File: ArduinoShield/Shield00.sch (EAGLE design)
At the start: 28 parts

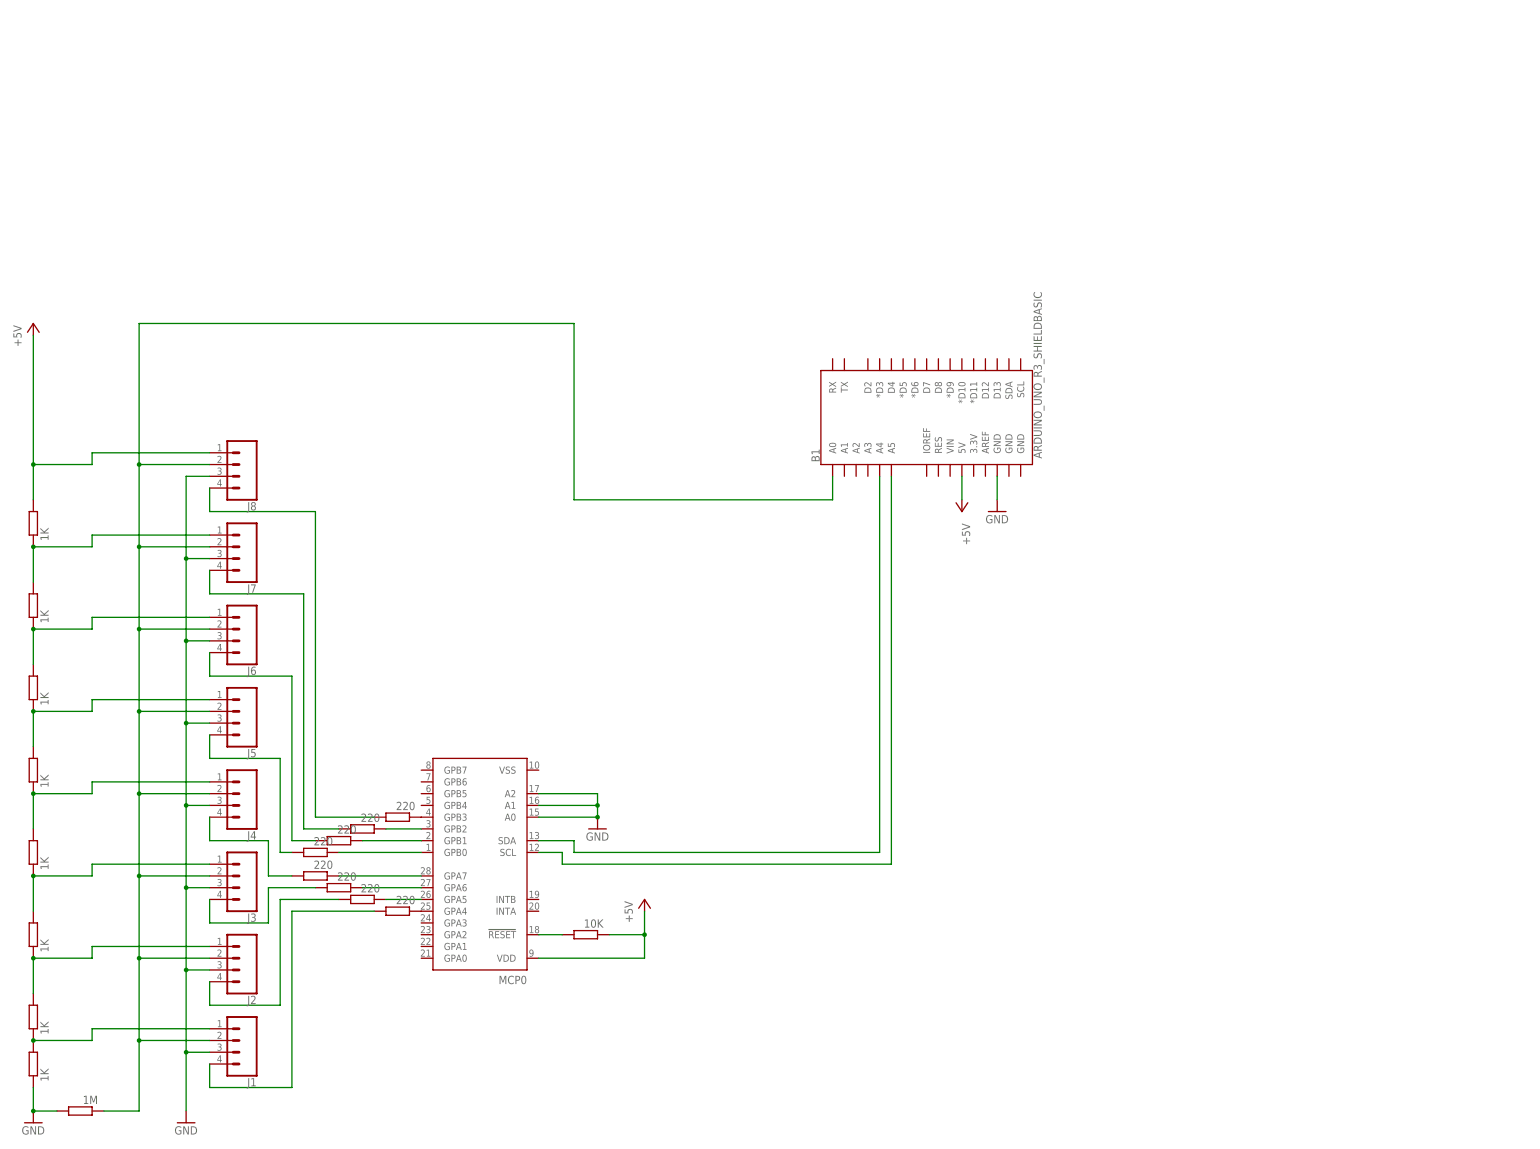
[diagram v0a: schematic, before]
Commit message: add mp3, mcp1 et 2 and pumplevel
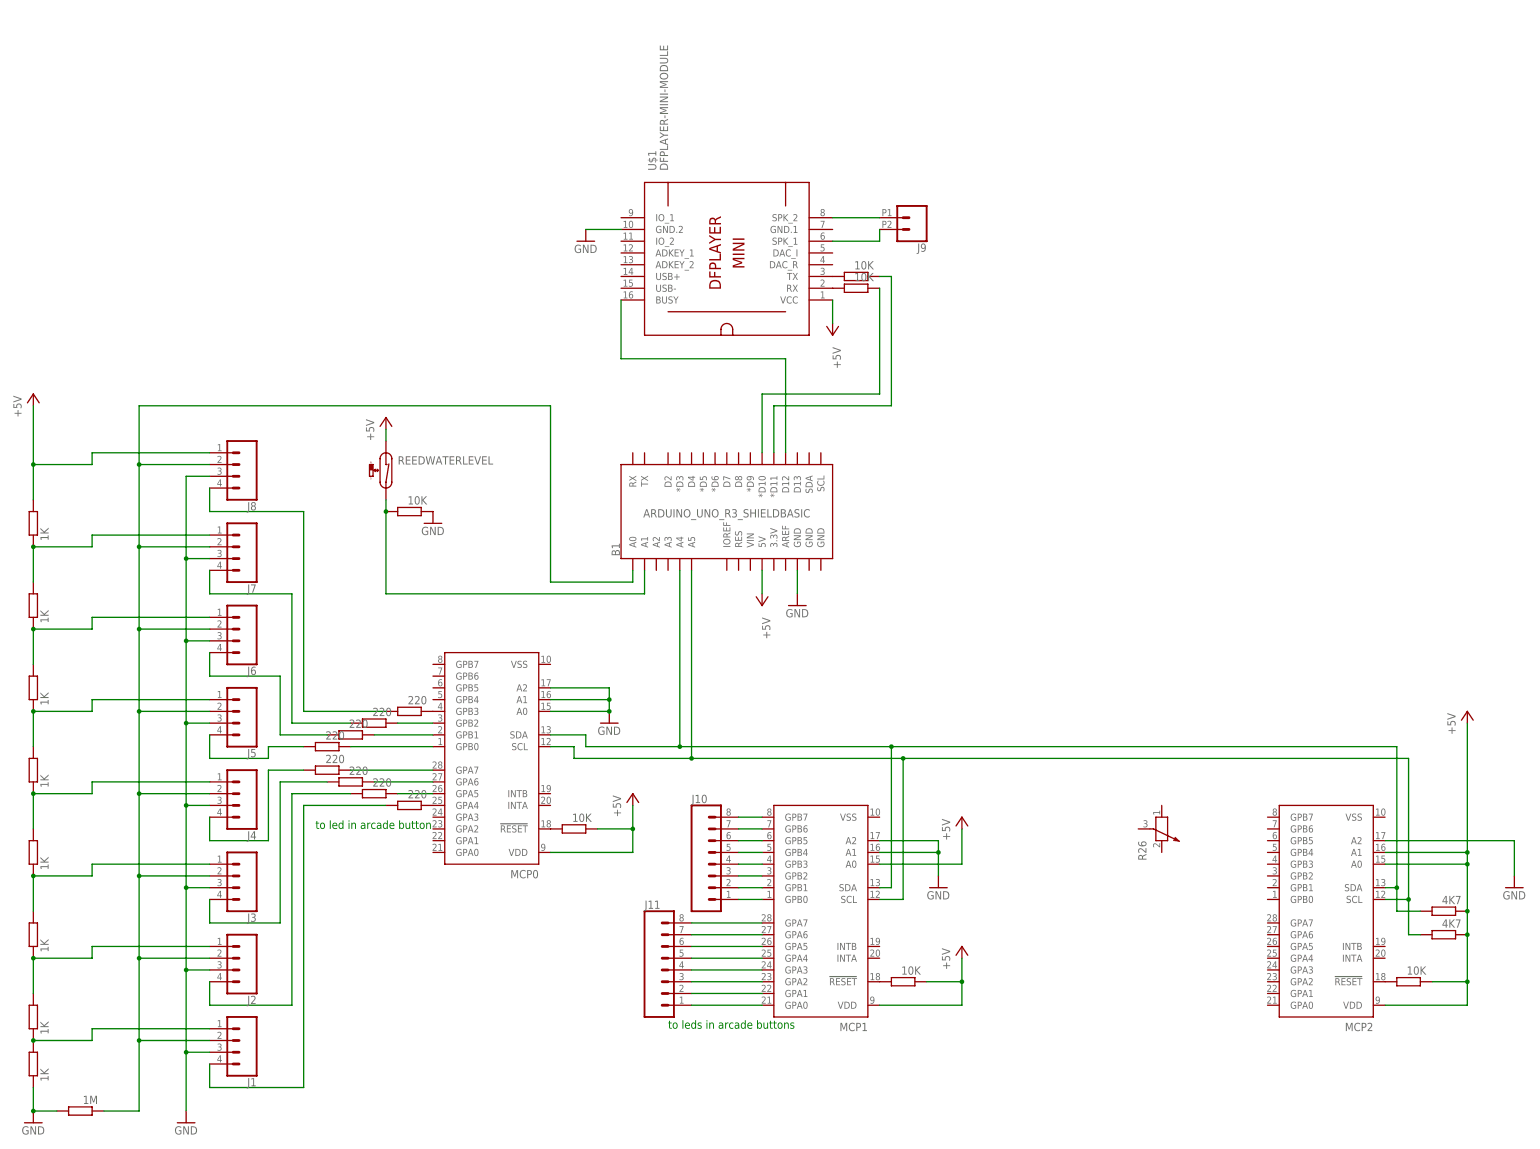
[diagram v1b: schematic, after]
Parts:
- added J10, J11: (no value), SparkFun-Connectors:CONN_08"
- added J9: (no value), SparkFun-Connectors:CONN_022.54MM_SCREWTERM
- added MCP1, MCP2: MCP23017SO, microchip:MCP23017SO
- added R10, R19, R21, R22, R23: 10K, rcl:R-EU_R0805
- added R24, R25: 4K7, rcl:R-EU_R0805
- added R26: (no value), rcl:POTENTIOMETER_PT-10
- added REEDWATERLEVEL: REED-SWITCH-MK6-5-B, switch-reed:REED-SWITCH-MK6-5-B
- added U$1: DFPLAYER-MINI-MODULE, diy-modules:DFPLAYER-MINI-MODULE
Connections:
- new net N$18: B1.A4, MCP0.SDA, MCP1.SDA, MCP2.SDA, R24.2
- new net N$26: J9.1, U$1.SPK_2
- new net N$27: J9.2, U$1.SPK_1
- new net N$28: R10.2, U$1.TX
- new net N$32: B1.*D10, R19.1
- new net N$33: B1.*D11, R10.1
- new net N$34: B1.D12, U$1.BUSY
- new net N$35: MCP1.!RESET, R22.2
- new net N$36: B1.A1, R21.2, REEDWATERLEVEL.2
- new net N$37: J10.5, MCP1.GPB4
- new net N$38: J10.4, MCP1.GPB3
- new net N$39: J10.3, MCP1.GPB2
- new net N$40: J10.2, MCP1.GPB1
- new net N$41: J10.1, MCP1.GPB0
- new net N$42: J11.8, MCP1.GPA7
- new net N$43: J11.7, MCP1.GPA6
- new net N$44: J11.6, MCP1.GPA5
- new net N$45: J11.5, MCP1.GPA4
- new net N$46: J11.4, MCP1.GPA3
- new net N$47: J11.3, MCP1.GPA2
- new net N$48: J11.2, MCP1.GPA1
- new net N$49: J11.1, MCP1.GPA0
- new net N$50: J10.6, MCP1.GPB5
- new net N$51: J10.7, MCP1.GPB6
- new net N$52: J10.8, MCP1.GPB7
- new net N$55: MCP2.!RESET, R23.2
- net +5V: now also MCP1.A0, MCP1.VDD, MCP2.A0, MCP2.A1, MCP2.VDD, R22.1, R23.1, R24.1, R25.1, REEDWATERLEVEL.1, U$1.VCC
- net GND: now also MCP1.A1, MCP1.A2, MCP2.A2, R21.1, U$1.GND.2
- net N$29: now also MCP1.SCL, MCP2.SCL, R25.2
- net N$31: now also R19.2, U$1.RX; no longer B1.A4, MCP0.SDA
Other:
- note added: "to led in arcade button"
- note added: "to leds in arcade buttons"
- moved on the sheet: B1, MCP0

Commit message: end v1 schemboard
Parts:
- removed J10: (no value), SparkFun-Connectors:CONN_08"
- added J12: (no value), SparkFun-Connectors:CONN_08"
- added LED1, LED2, LED3, LED4, LED5, LED7: (no value), led:LED5MM
- added R27, R28, R29, R30, R31, R32, R33, R34, R35, R36, R37, R38, R39, R40, R41, R42: 10K, rcl:R-EU_R0805
- added R43, R44, R45, R46, R48: (no value), rcl:POTENTIOMETER_PT-10
- added T1, T10, T11, T12, T13, T14, T15, T16, T2, T3, T4, T5, T6, T7, T8, T9: BC337, transistor:BC337
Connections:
- new net N$53: R34.1, T8.B
- new net N$54: R36.1, T10.B
- new net N$56: R37.1, T11.B
- new net N$57: R38.1, T12.B
- new net N$58: R39.1, T13.B
- new net N$59: R40.1, T14.B
- new net N$60: R41.1, T15.B
- new net N$61: R42.1, T16.B
- new net N$62: MCP1.GPA7, R34.2
- new net N$63: MCP1.GPA6, R33.2
- new net N$64: MCP1.GPA5, R32.2
- new net N$65: MCP1.GPA4, R31.2
- new net N$66: MCP1.GPA3, R30.2
- new net N$67: MCP1.GPA2, R29.2
- new net N$68: MCP1.GPA1, R28.2
- new net N$69: MCP1.GPA0, R27.2
- new net N$70: J11.4, T4.C
- new net N$71: J11.5, T5.C
- new net N$72: J11.6, T6.C
- new net N$73: J11.7, T7.C
- new net N$74: J11.8, T8.C
- new net N$75: J11.3, T3.C
- new net N$76: J11.2, T2.C
- new net N$77: J11.1, T1.C
- new net N$78: J12.4, T12.C
- new net N$79: J12.5, T13.C
- new net N$80: J12.6, T14.C
- new net N$81: J12.7, T15.C
- new net N$82: J12.8, T16.C
- new net N$83: J12.3, T11.C
- new net N$84: J12.2, T10.C
- new net N$85: J12.1, T9.C
- new net N$86: MCP2.GPA0, R48.1
- new net N$87: LED1.A, R26.3
- new net N$88: MCP2.GPA1, R26.1
- new net N$89: LED2.A, R43.3
- new net N$90: MCP2.GPA2, R43.1
- new net N$91: LED3.A, R44.3
- new net N$92: MCP2.GPA3, R44.1
- new net N$93: LED4.A, R45.3
- new net N$94: MCP2.GPA4, R45.1
- new net N$95: LED5.A, R46.3
- new net N$96: MCP2.GPA5, R46.1
- new net N$98: LED7.A, R48.3
- net GND: now also LED1.C, LED2.C, LED3.C, LED4.C, LED5.C, LED7.C, R26.2, R43.2, R44.2, R45.2, R46.2, R48.2, T1.E, T10.E, T11.E, T12.E, T13.E, T14.E, T15.E, T16.E, T2.E, T3.E, T4.E, T5.E, T6.E, T7.E, T8.E, T9.E
- net N$37: now also R39.2; no longer J10.5
- net N$38: now also R38.2; no longer J10.4
- net N$39: now also R37.2; no longer J10.3
- net N$40: now also R36.2; no longer J10.2
- net N$41: now also R35.2; no longer J10.1
- net N$42: now also R32.1, T6.B; no longer J11.8, MCP1.GPA7
- net N$43: now also R35.1, T9.B; no longer J11.7, MCP1.GPA6
- net N$44: now also R27.1, T1.B; no longer J11.6, MCP1.GPA5
- net N$45: now also R28.1, T2.B; no longer J11.5, MCP1.GPA4
- net N$46: now also R30.1, T4.B; no longer J11.4, MCP1.GPA3
- net N$47: now also R29.1, T3.B; no longer J11.3, MCP1.GPA2
- net N$48: now also R31.1, T5.B; no longer J11.2, MCP1.GPA1
- net N$49: now also R33.1, T7.B; no longer J11.1, MCP1.GPA0
- net N$50: now also R40.2; no longer J10.6
- net N$51: now also R41.2; no longer J10.7
- net N$52: now also R42.2; no longer J10.8
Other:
- note added: "To relays, 2x module 8"
- note removed: "to leds in arcade buttons"
- moved on the sheet: J11, MCP1, MCP2, R26

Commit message: pump still not working
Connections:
- net N$36: now also B1.D8; no longer B1.A1
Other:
- moved on the sheet: REEDWATERLEVEL
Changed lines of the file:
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@@
 <attribute name="VALUE" x="375.92" y="106.68" size="1.778" layer="96"/>
 </instance>
-<instance part="REEDWATERLEVEL" gate="G$1" x="289.56" y="137.16" smashed="yes">
-<attribute name="NAME" x="292.1" y="139.7" size="1.778" layer="95"/>
+<instance part="REEDWATERLEVEL" gate="G$1" x="287.02" y="193.04" smashed="yes">
+<attribute name="NAME" x="289.56" y="195.58" size="1.778" layer="95"/>
 </instance>
 <instance part="U$1" gate="G$1" x="363.22" y="185.42" smashed="yes" rot="R90">
@@
 <attribute name="VALUE" x="330.2" y="185.42" size="1.778" layer="96"/>
 </instance>
-<instance part="P+5" gate="1" x="289.56" y="149.86" smashed="yes">
-<attribute name="VALUE" x="287.02" y="144.78" size="1.778" layer="96" rot="R90"/>
-</instance>
-<instance part="R21" gate="G$1" x="294.64" y="129.54" smashed="yes" rot="R180">
-<attribute name="NAME" x="298.45" y="128.0414" size="1.778" layer="95" rot="R180" display="off"/>
-<attribute name="VALUE" x="298.45" y="132.842" size="1.778" layer="96" rot="R180"/>
-</instance>
-<instance part="GND6" gate="1" x="299.72" y="127" smashed="yes">
-<attribute name="VALUE" x="297.18" y="124.46" size="1.778" layer="96"/>
+<instance part="P+5" gate="1" x="287.02" y="205.74" smashed="yes">
+<attribute name="VALUE" x="284.48" y="200.66" size="1.778" layer="96" rot="R90"/>
+</instance>
+<instance part="R21" gate="G$1" x="292.1" y="185.42" smashed="yes" rot="R180">
+<attribute name="NAME" x="295.91" y="183.9214" size="1.778" layer="95" rot="R180" display="off"/>
+<attribute name="VALUE" x="295.91" y="188.722" size="1.778" layer="96" rot="R180"/>
+</instance>
+<instance part="GND6" gate="1" x="297.18" y="182.88" smashed="yes">
+<attribute name="VALUE" x="294.64" y="180.34" size="1.778" layer="96"/>
 </instance>
 <instance part="MCP1" gate="G$1" x="414.02" y="10.16" smashed="yes" rot="R180">
@@
 <segment>
 <pinref part="REEDWATERLEVEL" gate="G$1" pin="1"/>
-<wire x1="289.56" y1="144.78" x2="289.56" y2="147.32" width="0.1524" layer="91"/>
+<wire x1="287.02" y1="200.66" x2="287.02" y2="203.2" width="0.1524" layer="91"/>
 <pinref part="P+5" gate="1" pin="+5V"/>
 </segment>
@@
 <segment>
 <pinref part="REEDWATERLEVEL" gate="G$1" pin="2"/>
-<wire x1="289.56" y1="132.08" x2="289.56" y2="129.54" width="0.1524" layer="91"/>
-<pinref part="B1" gate="G$1" pin="A1"/>
-<wire x1="289.56" y1="129.54" x2="289.56" y2="111.76" width="0.1524" layer="91"/>
-<wire x1="289.56" y1="111.76" x2="345.44" y2="111.76" width="0.1524" layer="91"/>
-<wire x1="345.44" y1="111.76" x2="345.44" y2="116.84" width="0.1524" layer="91"/>
+<wire x1="287.02" y1="187.96" x2="287.02" y2="185.42" width="0.1524" layer="91"/>
+<wire x1="287.02" y1="185.42" x2="287.02" y2="154.94" width="0.1524" layer="91"/>
 <pinref part="R21" gate="G$1" pin="2"/>
-<junction x="289.56" y="129.54"/>
-</segment>
-</net>
+<junction x="287.02" y="185.42"/>
+<wire x1="287.02" y1="154.94" x2="365.76" y2="154.94" width="0.1524" layer="91"/>
+<pinref part="B1" gate="G$1" pin="D8"/>
+<wire x1="365.76" y1="154.94" x2="365.76" y2="142.24" width="0.1524" layer="91"/>
+</segment>
+</net>

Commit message: add relais 0-16
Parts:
- added IRFZ44N: IRF840, transistor-fet:IRF840
- added SP1: SMS-1308MS-2-R, speaker:SMS-1308MS-2-R
- added STRIPLED: (no value), led:LED5MM
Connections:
- new net +12V: STRIPLED.A
- new net N$100: IRFZ44N.D, STRIPLED.C
- new net N$97: B1.*D9, IRFZ44N.G
- net GND: now also IRFZ44N.S
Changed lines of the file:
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@@
 <part name="R46" library="rcl" library_urn="urn:adsk.eagle:library:334" deviceset="POTENTIOMETER_" device="PT-10" package3d_urn="urn:adsk.eagle:package:23786/1"/>
 <part name="LED5" library="led" library_urn="urn:adsk.eagle:library:259" deviceset="LED" device="5MM" package3d_urn="urn:adsk.eagle:package:15799/2"/>
+<part name="IRFZ44N" library="transistor-fet" library_urn="urn:adsk.eagle:library:396" deviceset="IRF840" device="" package3d_urn="urn:adsk.eagle:package:28520/1"/>
+<part name="SP1" library="speaker" library_urn="urn:adsk.eagle:library:365" deviceset="SMS-1308MS-2-R" device="" package3d_urn="urn:adsk.eagle:package:26519/1"/>
+<part name="STRIPLED" library="led" library_urn="urn:adsk.eagle:library:259" deviceset="LED" device="5MM" package3d_urn="urn:adsk.eagle:package:15799/2"/>
+<part name="P+8" library="supply1" library_urn="urn:adsk.eagle:library:371" deviceset="+12V" device=""/>
+<part name="GND12" library="supply1" library_urn="urn:adsk.eagle:library:371" deviceset="GND" device=""/>
 </parts>
 <sheets>
@@
 <attribute name="NAME" x="483.616" y="8.128" size="1.778" layer="95" rot="R90"/>
 <attribute name="VALUE" x="485.775" y="8.128" size="1.778" layer="96" rot="R90"/>
+</instance>
+<instance part="IRFZ44N" gate="G$1" x="457.2" y="160.02" smashed="yes">
+<attribute name="NAME" x="445.77" y="162.56" size="1.778" layer="95"/>
+</instance>
+<instance part="SP1" gate="A" x="414.02" y="193.04" smashed="yes">
+<attribute name="NAME" x="419.1" y="194.31" size="1.778" layer="95"/>
+<attribute name="VALUE" x="419.1" y="190.5" size="1.778" layer="96"/>
+</instance>
+<instance part="STRIPLED" gate="G$1" x="464.82" y="175.26" smashed="yes">
+<attribute name="NAME" x="468.376" y="170.688" size="1.778" layer="95" rot="R90"/>
+<attribute name="VALUE" x="470.535" y="170.688" size="1.778" layer="96" rot="R90"/>
+</instance>
+<instance part="P+8" gate="1" x="464.82" y="187.96" smashed="yes">
+<attribute name="VALUE" x="462.28" y="182.88" size="1.778" layer="96" rot="R90"/>
+</instance>
+<instance part="GND12" gate="1" x="462.28" y="152.4" smashed="yes">
+<attribute name="VALUE" x="459.74" y="149.86" size="1.778" layer="96"/>
 </instance>
 </instances>
@@
 <junction x="480.06" y="7.62"/>
 </segment>
+<segment>
+<pinref part="IRFZ44N" gate="G$1" pin="S"/>
+<wire x1="462.28" y1="157.48" x2="462.28" y2="154.94" width="0.1524" layer="91"/>
+<pinref part="GND12" gate="1" pin="GND"/>
+</segment>
 </net>
 <net name="N$1" class="0">
@@
 </segment>
 </net>
+<net name="N$97" class="0">
+<segment>
+<pinref part="B1" gate="G$1" pin="*D9"/>
+<wire x1="368.3" y1="142.24" x2="368.3" y2="157.48" width="0.1524" layer="91"/>
+<wire x1="368.3" y1="157.48" x2="452.12" y2="157.48" width="0.1524" layer="91"/>
+<pinref part="IRFZ44N" gate="G$1" pin="G"/>
+</segment>
+</net>
+<net name="N$100" class="0">
+<segment>
+<pinref part="IRFZ44N" gate="G$1" pin="D"/>
+<wire x1="462.28" y1="162.56" x2="464.82" y2="162.56" width="0.1524" layer="91"/>
+<wire x1="464.82" y1="162.56" x2="464.82" y2="170.18" width="0.1524" layer="91"/>
+<pinref part="STRIPLED" gate="G$1" pin="C"/>
+</segment>
+</net>
+<net name="+12V" class="0">
+<segment>
+<pinref part="STRIPLED" gate="G$1" pin="A"/>
+<pinref part="P+8" gate="1" pin="+12V"/>
+<wire x1="464.82" y1="177.8" x2="464.82" y2="185.42" width="0.1524" layer="91"/>
+</segment>
+</net>

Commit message: delete mcp2, add leds controls
assez de pins sur arduino pour les quelques leds qui restent à controler.
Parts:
- removed LED1, LED2, LED3, LED4, LED5, LED7: (no value), led:LED5MM
- removed MCP2: MCP23017SO, microchip:MCP23017SO
- removed R23: 10K, rcl:R-EU_R0805
- removed R26, R43, R44, R45, R46, R48: (no value), rcl:POTENTIOMETER_PT-10
- added IRFZ44N1, IRFZ44N2: IRF840, transistor-fet:IRF840
- added LED10, LED6, LED8, LED9, NAPPE-LED, NAPPE-LED1, NAPPE-LED10, NAPPE-LED11, NAPPE-LED12, NAPPE-LED2, NAPPE-LED3, NAPPE-LED4, NAPPE-LED5, NAPPE-LED6, NAPPE-LED7, NAPPE-LED8, NAPPE-LED9: (no value), led:LED5MM
- added R47, R49, R50, R51: 68, rcl:R-EU_R0805
- added R52: 100, rcl:R-EU_R0805
- added R53, R54, R55, R56: (no value), rcl:POTENTIOMETER_PT-10
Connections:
- removed net N$55: MCP2.!RESET, R23.2
- removed net N$86: MCP2.GPA0, R48.1
- removed net N$87: LED1.A, R26.3
- removed net N$88: MCP2.GPA1, R26.1
- removed net N$89: LED2.A, R43.3
- removed net N$90: MCP2.GPA2, R43.1
- removed net N$91: LED3.A, R44.3
- removed net N$92: MCP2.GPA3, R44.1
- removed net N$93: LED4.A, R45.3
- removed net N$94: MCP2.GPA4, R45.1
- removed net N$95: LED5.A, R46.3
- removed net N$96: MCP2.GPA5, R46.1
- removed net N$98: LED7.A, R48.3
- new net N$101: B1.*D6, IRFZ44N1.G
- new net N$102: NAPPE-LED.A, NAPPE-LED1.C
- new net N$103: IRFZ44N2.D
- new net N$104: NAPPE-LED1.A, NAPPE-LED2.C
- new net N$105: NAPPE-LED2.A, R47.2
- new net N$106: NAPPE-LED10.C, NAPPE-LED9.A
- new net N$107: NAPPE-LED3.A, NAPPE-LED4.C
- new net N$108: NAPPE-LED4.A, NAPPE-LED5.C
- new net N$109: NAPPE-LED5.A, R49.2
- new net N$110: NAPPE-LED10.A, NAPPE-LED11.C
- new net N$111: NAPPE-LED6.A, NAPPE-LED7.C
- new net N$112: NAPPE-LED7.A, NAPPE-LED8.C
- new net N$113: NAPPE-LED8.A, R50.2
- new net N$114: NAPPE-LED11.A, R51.2
- new net N$115: NAPPE-LED9.C
- new net N$116: B1.*D5, IRFZ44N2.G
- new net N$117: B1.D4, R52.2
- new net N$118: NAPPE-LED12.A, R52.1
- new net N$121: B1.D2, R53.1
- new net N$122: LED6.A, R53.3
- new net N$124: LED8.A, R54.3
- new net N$125: B1.*D3, R54.1
- new net N$127: LED9.A, R55.3
- new net N$128: B1.D8, R55.1
- new net N$129: LED10.A, R56.3
- new net N$130: B1.D13, R56.1
- new net N$99: IRFZ44N1.D, NAPPE-LED.C, NAPPE-LED3.C, NAPPE-LED6.C
- net +12V: now also R47.1, R49.1, R50.1, R51.1
- net +5V: no longer MCP2.A0, MCP2.A1, MCP2.VDD, R23.1
- net GND: now also IRFZ44N1.S, IRFZ44N2.S, LED10.C, LED6.C, LED8.C, LED9.C, NAPPE-LED12.C, R53.2, R54.2, R55.2, R56.2; no longer LED1.C, LED2.C, LED3.C, LED4.C, LED5.C, LED7.C, MCP2.A2, R26.2, R43.2, R44.2, R45.2, R46.2, R48.2
- net N$18: now also R25.2; no longer MCP2.SDA, R24.2
- net N$29: now also R24.2; no longer MCP2.SCL, R25.2
- net N$36: now also B1.D7; no longer B1.D8
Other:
- moved on the sheet: IRFZ44N, J11, J12, J9, MCP1, REEDWATERLEVEL, SP1, STRIPLED, U$1

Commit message: last leds control, shield completed
Version1, hopeSO
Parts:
- added LED1: (no value), led:LED5MM
- added R23: (no value), rcl:POTENTIOMETER_PT-10
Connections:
- removed net N$103: IRFZ44N2.D
- new net N$55: LED1.A, R23.3
- new net N$86: B1.RX, R23.1
- net GND: now also LED1.C, R23.2
- net N$101: now also B1.D7; no longer B1.*D6
- net N$115: now also IRFZ44N2.D
- net N$116: now also B1.*D6; no longer B1.*D5
- net N$117: now also B1.*D5; no longer B1.D4
- net N$121: now also B1.TX; no longer B1.D2
- net N$125: now also B1.D2; no longer B1.*D3
- net N$128: now also B1.*D3; no longer B1.D8
- net N$130: now also B1.D4; no longer B1.D13
- net N$2: now also B1.A3; no longer B1.A0
- net N$36: now also B1.D13; no longer B1.D7
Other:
- moved on the sheet: B1, IRFZ44N, IRFZ44N1, LED10, LED6, LED8, LED9, NAPPE-LED, R53, R54, R55, R56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
